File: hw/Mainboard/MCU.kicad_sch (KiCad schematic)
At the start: 70 parts, among them J12 NOT_HDMI_A, J13 Micro_SD, J14 USB2.0_HOST_TYPE_C, J15 DEBUG, J16 MCU, J17 BOOTSEL, SW2 MCU_RESET, SW3 MENU, U14 RP2040, U16 W25Q128JVS, Y1 12 MHz

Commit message: hw: wip
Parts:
- NT6: footprint PET:NetTie-2_SMD_Pad_0.4_to_0.2mm -> PET:NetTie-2_SMD_Pad_0.4_to_0.28mm
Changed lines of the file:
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@@
       (effects (font (size 1.27 1.27)) hide)
     )
-    (property "Footprint" "PET:NetTie-2_SMD_Pad_0.4_to_0.2mm" (id 2) (at 374.65 35.56 0)
+    (property "Footprint" "PET:NetTie-2_SMD_Pad_0.4_to_0.28mm" (id 2) (at 374.65 35.56 0)
       (effects (font (size 1.27 1.27)) hide)
     )

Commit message: hw: wip
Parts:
- NT41, NT42: symbol PET:PowerTie_2 -> Device:NetTie_2
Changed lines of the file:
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@@
     (pin "2")
   )
-  (symbol (lib_id "PET:PowerTie_2") (at 236.22 55.88 0) (mirror y) (unit 1)
+  (symbol (lib_id "Device:NetTie_2") (at 236.22 55.88 0) (mirror y) (unit 1)
     (in_bom yes) (on_board yes)
     (property "Reference" "NT42" (id 0) (at 236.22 53.34 0)
@@
     (pin "2")
   )
-  (symbol (lib_id "PET:PowerTie_2") (at 226.06 53.34 0) (mirror y) (unit 1)
+  (symbol (lib_id "Device:NetTie_2") (at 226.06 53.34 0) (mirror y) (unit 1)
     (in_bom yes) (on_board yes)
     (property "Reference" "NT41" (id 0) (at 226.06 50.8 0)

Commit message: jlcpcb - 1/19
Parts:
- removed NT42: +3V3, PET:NetTie-2_SMD_Pad_1.6_to_0.4mm, symbol Device:NetTie_2
- added C83, C84: 100n, Capacitor_SMD:C_0402_1005Metric, symbol Device:C_Small
- added J22: MENU, Connector_PinHeader_2.54mm:PinHeader_1x02_P2.54mm_Vertical, symbol Connector:Conn_01x02_Male
- C37, C38: value 2.2u -> 2.2u 6.3V
- C47, C48: value 30p -> 30p 50V
- D10: value STS_GRN -> LED_GRN
- J14: Spec https://www.usb.org/sites/default/files/documents/usb_type-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 -> (none)
- R35, R36: value 5k1 -> 22k; LCSC C25905 -> C25768
- SW2: value MCU_RESET -> RUN; Alt-LCSC (none) -> C457531; LCSC C457531 -> (none)
- SW3: Alt-LCSC (none) -> C139765; LCSC C139765 -> (none)
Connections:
- net GND: now also C84.2, J22.1 (Pin_1)
- net GP27: now also C84.1, J22.2 (Pin_2)
- net PD_GND: now also J14.A12_B1 (GND), J14.A1_B12 (GND), J14.S1 (SHIELD), NT19.2, NT21.2, C83.2
- net RUN: now also C83.1
- net VBUS: now reaches J14.A9_B4 (VBUS), NT20.2, R36.1
- net VBUS: now also J14.A4_B9 (VBUS), NT18.2, R35.1
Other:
- note added: "CEC and I2C are for possible future use. DANGER: Closing the SCL/SDA jumpers pulls the corresponding GPIO pins to +5V. Only do this if you know what you're doing."
- note added: "DAT0 (RX) is open collector and gets stronger pullup. DAT[3:1] are inputs on powerup and get weak pullups to avoid excessive current draw due to metastablitiy."
- note added: "Rp = 22k -> 1.5A @ 5V"
- note added: "~{SPI_ENA} is driven low during FPGA programming. We use this to hold the MCU in reset when updating the FPGA to avoid contention on SPI pins. FT2232HL can source ~16ma, so 1K should be ok."
- note removed: "DAT0 (RX) is open collector and gets stronger pullup. DAT[3:1] are inputs on powerup and get weaker pullups to avoid excessive current draw due to metastablitiy."
- note removed: "~{SPI_ENA} is driven low during FPGA programming. We use this to hold the MCU in reset when programming to avoid contention on SPI pins. FT2232HL can source ~16ma, so 1K should be ok."
- moved on the sheet: SW2, SW3

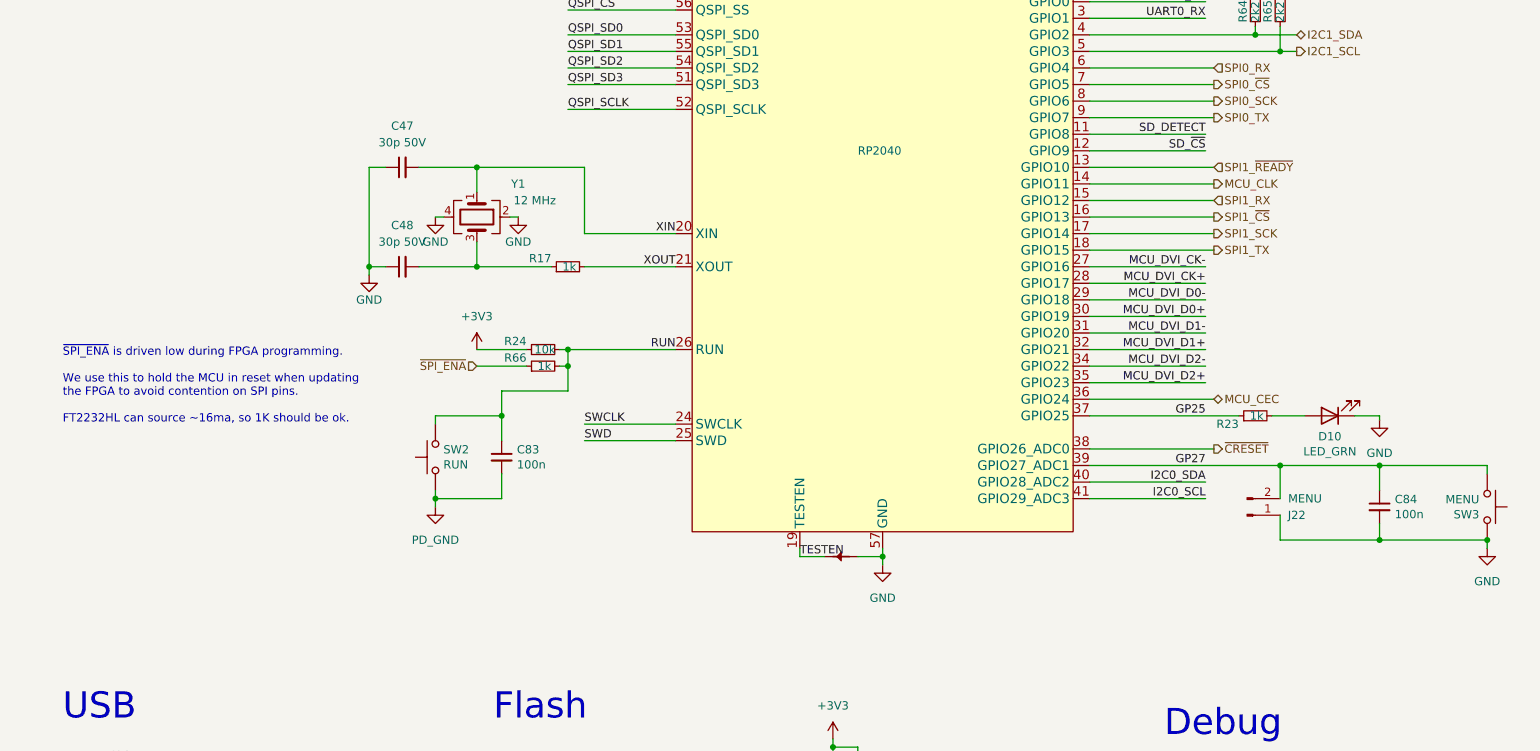
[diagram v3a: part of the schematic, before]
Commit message: hw: drive CRESET through 10k, remove TDO pullup
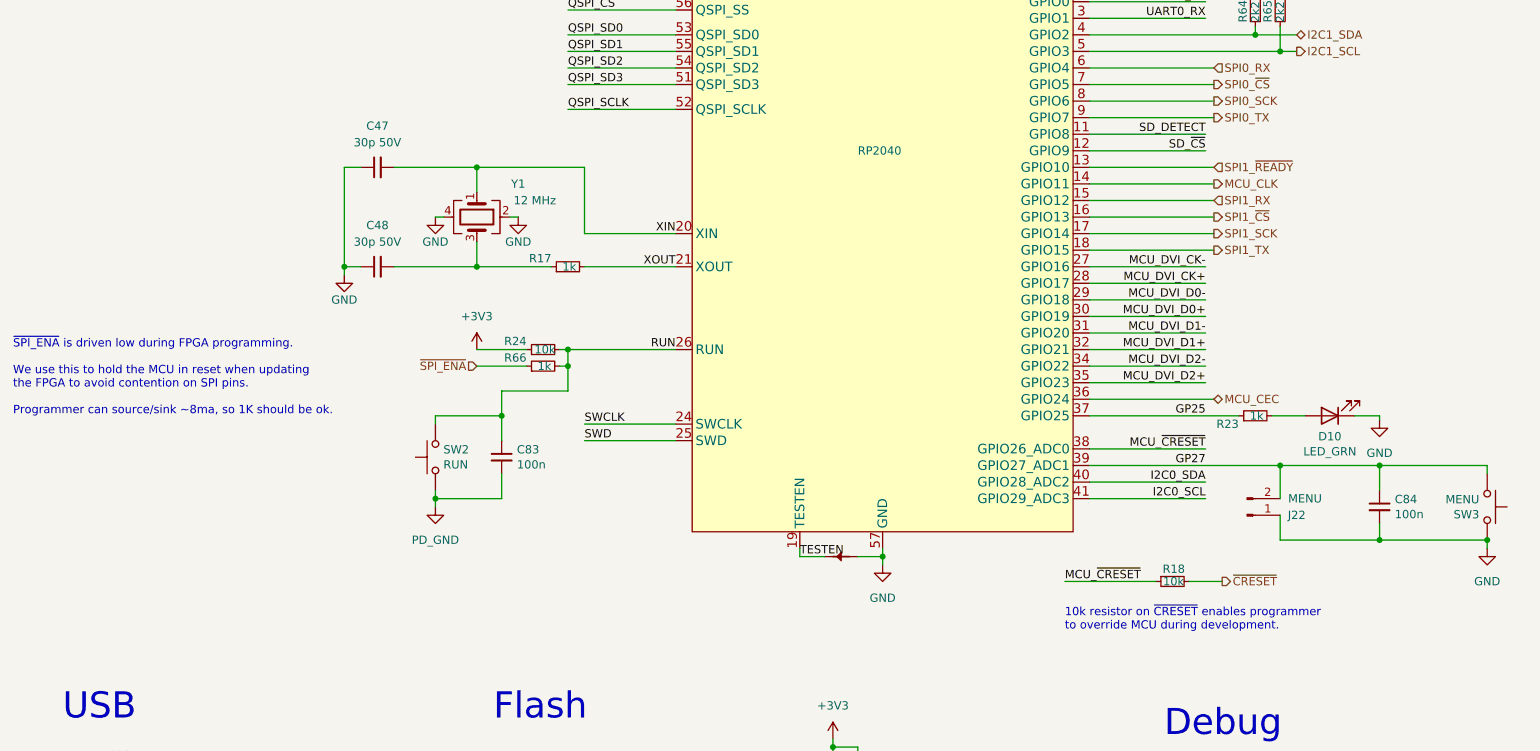
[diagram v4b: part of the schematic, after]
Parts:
- added R18: 10k, Resistor_SMD:R_0402_1005Metric, symbol Device:R_Small
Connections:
- net ~{CRESET}: now also R18.2; no longer U14.38 (GPIO26_ADC0)
- new net MCU_~{CRESET}: R18.1, U14.38 (GPIO26_ADC0)
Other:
- note added: "10k resistor on ~{CRESET} enables programmer to override MCU during development."
- note added: "~{SPI_ENA} is driven low during FPGA programming. We use this to hold the MCU in reset when updating the FPGA to avoid contention on SPI pins. Programmer can source/sink ~8ma, so 1K should be ok."
- note removed: "~{SPI_ENA} is driven low during FPGA programming. We use this to hold the MCU in reset when updating the FPGA to avoid contention on SPI pins. FT2232HL can source ~16ma, so 1K should be ok."
- moved on the sheet: C47, C48
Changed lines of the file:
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@@
   (junction (at 201.93 63.5) (diameter 0) (color 0 0 0 0)
   )
-  (junction (at 82.55 125.73) (diameter 0) (color 0 0 0 0)
+  (junction (at 78.74 125.73) (diameter 0) (color 0 0 0 0)
   )
   (junction (at 322.58 87.63) (diameter 0) (color 0 0 0 0)
@@
     (stroke (width 0) (type default) (color 0 0 0 0))
   )
-  (wire (pts (xy 90.17 125.73) (xy 99.06 125.73))
+  (wire (pts (xy 86.36 125.73) (xy 99.06 125.73))
     (stroke (width 0) (type default) (color 0 0 0 0))
   )
@@
     (stroke (width 0) (type default) (color 0 0 0 0))
   )
-  (wire (pts (xy 90.17 110.49) (xy 99.06 110.49))
+  (wire (pts (xy 86.36 110.49) (xy 99.06 110.49))
     (stroke (width 0) (type default) (color 0 0 0 0))
   )
@@
     (stroke (width 0) (type default) (color 0 0 0 0))
   )
-  (wire (pts (xy 82.55 110.49) (xy 82.55 125.73))
+  (wire (pts (xy 189.23 173.99) (xy 203.2 173.99))
+    (stroke (width 0) (type default) (color 0 0 0 0))
+  )
+  (wire (pts (xy 78.74 110.49) (xy 78.74 125.73))
     (stroke (width 0) (type default) (color 0 0 0 0))
   )
@@
     (stroke (width 0) (type default) (color 0 0 0 0))
   )
-  (wire (pts (xy 82.55 125.73) (xy 85.09 125.73))
+  (wire (pts (xy 78.74 125.73) (xy 81.28 125.73))
     (stroke (width 0) (type default) (color 0 0 0 0))
   )
@@
     (stroke (width 0) (type default) (color 0 0 0 0))
   )
-  (wire (pts (xy 193.04 153.67) (xy 212.09 153.67))
-    (stroke (width 0) (type default) (color 0 0 0 0))
-  )
   (wire (pts (xy 215.9 214.63) (xy 227.33 214.63))
     (stroke (width 0) (type default) (color 0 0 0 0))
@@
     (stroke (width 0) (type default) (color 0 0 0 0))
   )
-  (wire (pts (xy 82.55 125.73) (xy 82.55 127))
+  (wire (pts (xy 78.74 125.73) (xy 78.74 127))
     (stroke (width 0) (type default) (color 0 0 0 0))
   )
@@
     (stroke (width 0) (type default) (color 0 0 0 0))
   )
-  (wire (pts (xy 85.09 110.49) (xy 82.55 110.49))
+  (wire (pts (xy 81.28 110.49) (xy 78.74 110.49))
     (stroke (width 0) (type default) (color 0 0 0 0))
   )
@@
     (stroke (width 0) (type default) (color 0 0 0 0))
   )
+  (wire (pts (xy 208.28 173.99) (xy 213.36 173.99))
+    (stroke (width 0) (type default) (color 0 0 0 0))
+  )
   (wire (pts (xy 66.04 207.01) (xy 66.04 209.55))
     (stroke (width 0) (type default) (color 0 0 0 0))
@@
   )
   (wire (pts (xy 314.96 158.75) (xy 314.96 160.02))
+    (stroke (width 0) (type default) (color 0 0 0 0))
+  )
+  (wire (pts (xy 193.04 153.67) (xy 210.82 153.67))
     (stroke (width 0) (type default) (color 0 0 0 0))
   )
@@
     (effects (font (size 4 4)) (justify left bottom))
   )
-  (text "~{SPI_ENA} is driven low during FPGA programming.\n\nWe use this to hold the MCU in reset when updating\nthe FPGA to avoid contention on SPI pins.\n\nFT2232HL can source ~16ma, so 1K should be ok."
-    (at 35.56 149.86 0)
+  (text "~{SPI_ENA} is driven low during FPGA programming.\n\nWe use this to hold the MCU in reset when updating\nthe FPGA to avoid contention on SPI pins.\n\nProgrammer can source/sink ~8ma, so 1K should be ok."
+    (at 27.94 148.59 0)
     (effects (font (size 1.27 1.27)) (justify left bottom))
   )
@@
     (effects (font (size 1.27 1.27)) (justify left bottom))
   )
+  (text "10k resistor on ~{CRESET} enables programmer\nto override MCU during development."
+    (at 189.23 181.61 0)
+    (effects (font (size 1.27 1.27)) (justify left bottom))
+  )
   (label "QSPI_SCLK" (at 125.73 223.52 0)
     (effects (font (size 1.27 1.27)) (justify left bottom))
@@
     (effects (font (size 1.27 1.27)) (justify right bottom))
   )
+  (label "MCU_~{CRESET}" (at 210.82 153.67 180)
+    (effects (font (size 1.27 1.27)) (justify right bottom))
+  )
   (label "DVI_D1-" (at 359.41 52.07 180)
     (effects (font (size 1.27 1.27)) (justify right bottom))
@@
   (label "USB_D+" (at 71.12 229.87 180)
     (effects (font (size 1.27 1.27)) (justify right bottom))
+  )
+  (label "MCU_~{CRESET}" (at 189.23 173.99 0)
+    (effects (font (size 1.27 1.27)) (justify left bottom))
   )
   (label "QSPI_SD0" (at 113.03 90.17 0)
@@
     (effects (font (size 1.27 1.27)) (justify left))
   )
+  (hierarchical_label "~{CRESET}" (shape output) (at 213.36 173.99 0)
+    (effects (font (size 1.27 1.27)) (justify left))
+  )
   (hierarchical_label "MCU_CEC" (shape bidirectional) (at 212.09 146.05 0)
     (effects (font (size 1.27 1.27)) (justify left))
@@
   )
   (hierarchical_label "SPI1_~{READY}" (shape input) (at 212.09 110.49 0)
-    (effects (font (size 1.27 1.27)) (justify left))
-  )
-  (hierarchical_label "~{CRESET}" (shape output) (at 212.09 153.67 0)
     (effects (font (size 1.27 1.27)) (justify left))
   )
@@
     (pin "1")
   )
-  (symbol (lib_id "Device:C_Small") (at 87.63 125.73 90) (unit 1)
+  (symbol (lib_id "Device:C_Small") (at 83.82 125.73 90) (unit 1)
     (in_bom yes) (on_board yes) (fields_autoplaced)
-    (property "Reference" "C48" (id 0) (at 87.6363 119.38 90))
-    (property "Value" "30p 50V" (id 1) (at 87.6363 121.92 90))
-    (property "Footprint" "Capacitor_SMD:C_0402_1005Metric" (id 2) (at 87.63 125.73 0)
-      (effects (font (size 1.27 1.27)) hide)
-    )
-    (property "Datasheet" "https://datasheet.lcsc.com/lcsc/1811141710_FH--Guangdong-Fenghua-Advanced-Tech-0402CG300J500NT_C1570.pdf" (id 3) (at 87.63 125.73 0)
-      (effects (font (size 1.27 1.27)) hide)
-    )
-    (property "LCSC" "C1570" (id 4) (at 87.63 125.73 0)
+    (property "Reference" "C48" (id 0) (at 83.8263 119.38 90))
+    (property "Value" "30p 50V" (id 1) (at 83.8263 121.92 90))
+    (property "Footprint" "Capacitor_SMD:C_0402_1005Metric" (id 2) (at 83.82 125.73 0)
+      (effects (font (size 1.27 1.27)) hide)
+    )
+    (property "Datasheet" "https://datasheet.lcsc.com/lcsc/1811141710_FH--Guangdong-Fenghua-Advanced-Tech-0402CG300J500NT_C1570.pdf" (id 3) (at 83.82 125.73 0)
+      (effects (font (size 1.27 1.27)) hide)
+    )
+    (property "LCSC" "C1570" (id 4) (at 83.82 125.73 0)
       (effects (font (size 1.27 1.27)) hide)
     )
@@
     (pin "2")
   )
-  (symbol (lib_id "Device:C_Small") (at 87.63 110.49 90) (unit 1)
+  (symbol (lib_id "Device:C_Small") (at 83.82 110.49 90) (unit 1)
     (in_bom yes) (on_board yes) (fields_autoplaced)
-    (property "Reference" "C47" (id 0) (at 87.6363 104.14 90))
-    (property "Value" "30p 50V" (id 1) (at 87.6363 106.68 90))
-    (property "Footprint" "Capacitor_SMD:C_0402_1005Metric" (id 2) (at 87.63 110.49 0)
-      (effects (font (size 1.27 1.27)) hide)
-    )
-    (property "Datasheet" "https://datasheet.lcsc.com/lcsc/1811141710_FH--Guangdong-Fenghua-Advanced-Tech-0402CG300J500NT_C1570.pdf" (id 3) (at 87.63 110.49 0)
-      (effects (font (size 1.27 1.27)) hide)
-    )
-    (property "LCSC" "C1570" (id 4) (at 87.63 110.49 0)
-      (effects (font (size 1.27 1.27)) hide)
-    )
-    (pin "1")
-    (pin "2")
-  )
-  (symbol (lib_id "power:GND") (at 82.55 127 0) (unit 1)
-    (in_bom yes) (on_board yes)
-    (property "Reference" "#PWR067" (id 0) (at 82.55 133.35 0)
-      (effects (font (size 1.27 1.27)) hide)
-    )
-    (property "Value" "GND" (id 1) (at 82.55 130.81 0))
-    (property "Footprint" "" (id 2) (at 82.55 127 0)
-      (effects (font (size 1.27 1.27)) hide)
-    )
-    (property "Datasheet" "" (id 3) (at 82.55 127 0)
+    (property "Reference" "C47" (id 0) (at 83.8263 104.14 90))
+    (property "Value" "30p 50V" (id 1) (at 83.8263 106.68 90))
+    (property "Footprint" "Capacitor_SMD:C_0402_1005Metric" (id 2) (at 83.82 110.49 0)
+      (effects (font (size 1.27 1.27)) hide)
+    )
+    (property "Datasheet" "https://datasheet.lcsc.com/lcsc/1811141710_FH--Guangdong-Fenghua-Advanced-Tech-0402CG300J500NT_C1570.pdf" (id 3) (at 83.82 110.49 0)
+      (effects (font (size 1.27 1.27)) hide)
+    )
+    (property "LCSC" "C1570" (id 4) (at 83.82 110.49 0)
+      (effects (font (size 1.27 1.27)) hide)
+    )
+    (pin "1")
+    (pin "2")
+  )
+  (symbol (lib_id "power:GND") (at 78.74 127 0) (unit 1)
+    (in_bom yes) (on_board yes)
+    (property "Reference" "#PWR067" (id 0) (at 78.74 133.35 0)
+      (effects (font (size 1.27 1.27)) hide)
+    )
+    (property "Value" "GND" (id 1) (at 78.74 130.81 0))
+    (property "Footprint" "" (id 2) (at 78.74 127 0)
+      (effects (font (size 1.27 1.27)) hide)
+    )
+    (property "Datasheet" "" (id 3) (at 78.74 127 0)
       (effects (font (size 1.27 1.27)) hide)
     )
@@
     (pin "1")
   )
+  (symbol (lib_id "Device:R_Small") (at 205.74 173.99 90) (mirror x) (unit 1)
+    (in_bom yes) (on_board yes)
+    (property "Reference" "R18" (id 0) (at 207.645 172.085 90)
+      (effects (font (size 1.27 1.27)) (justify left))
+    )
+    (property "Value" "10k" (id 1) (at 207.518 173.99 90)
+      (effects (font (size 1.27 1.27)) (justify left))
+    )
+    (property "Footprint" "Resistor_SMD:R_0402_1005Metric" (id 2) (at 205.74 173.99 0)
+      (effects (font (size 1.27 1.27)) hide)
+    )
+    (property "Datasheet" "https://datasheet.lcsc.com/lcsc/2206010100_UNI-ROYAL-Uniroyal-Elec-0402WGF1002TCE_C25744.pdf" (id 3) (at 205.74 173.99 0)
+      (effects (font (size 1.27 1.27)) hide)
+    )
+    (property "LCSC" "C25744" (id 4) (at 205.74 173.99 0)
+      (effects (font (size 1.27 1.27)) hide)
+    )
+    (pin "1")
+    (pin "2")
+  )
   (symbol (lib_id "power:GND") (at 106.68 62.23 0) (unit 1)

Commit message: hw: tidy power and resize pages
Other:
- title: (none) -> CBM PET Mainboard Replacement
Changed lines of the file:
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@@
 (kicad_sch (version 20211123) (generator eeschema)
-  (paper "B")
+  (paper "A")
+  (title_block
+    (title "CBM PET Mainboard Replacement")
+  )
   (junction (at 167.64 66.04) (diameter 0) (color 0 0 0 0)
   )
